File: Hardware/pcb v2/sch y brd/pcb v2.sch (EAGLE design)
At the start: 60 parts, among them J1 AVR_SPI_PRG_6PTH, J2 1981584-1, J3 HDMI, J4 HDMI, J5 JST-3, Q1 PMBT3904, Q2 PMBT3904, Q4 MC-306, U1 ATMEGA328P, U2 TXS0108EPWR-TSSOP20, U3 MB85RS16N, U4 ADP3338AKCZ-3.3RL7, U5 DS1307SO8, U6 BATTERYBATTERY1225_SMT, Y2 CSTCE16M0V53-R0 16MHZ

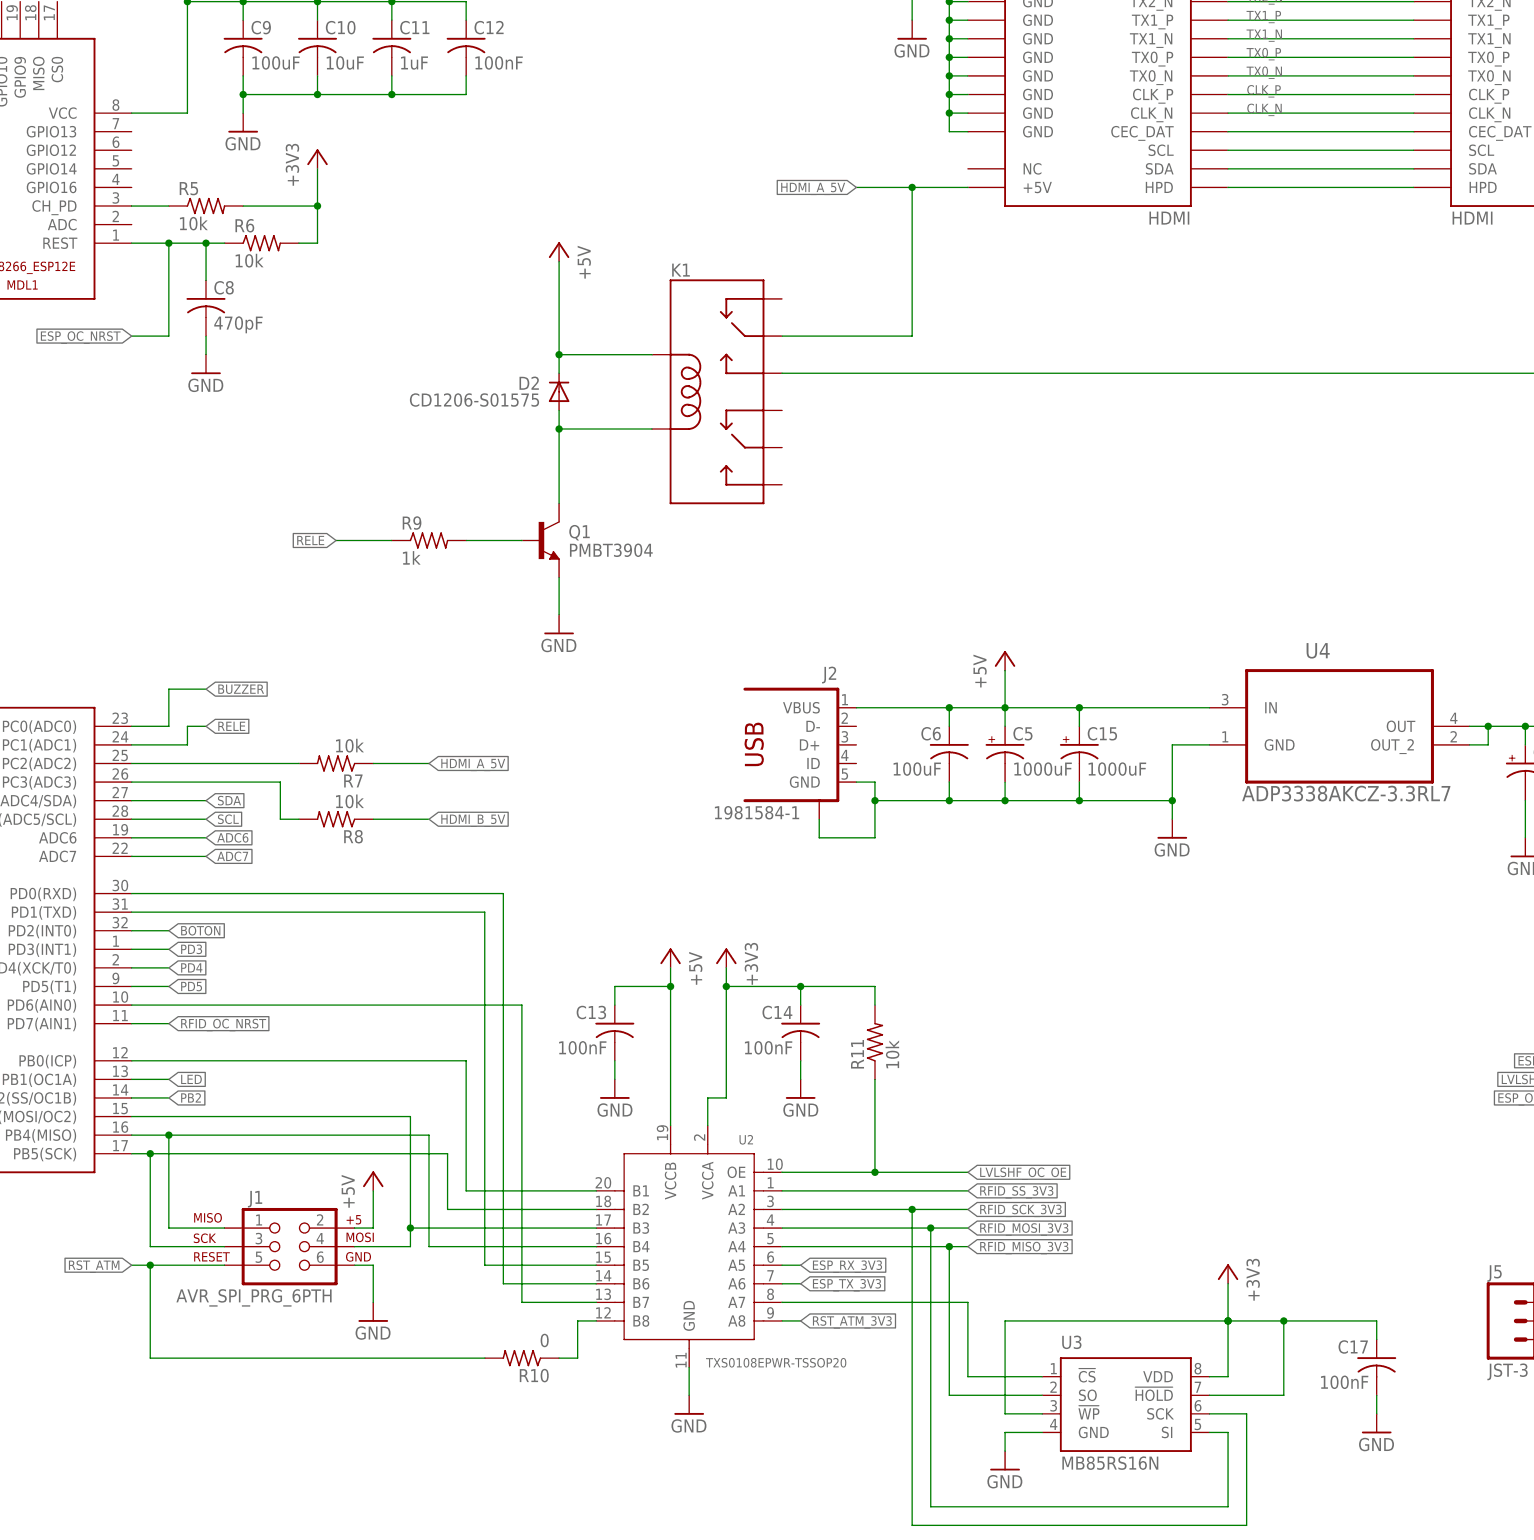
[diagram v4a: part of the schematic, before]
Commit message: ruteo hdmi completo
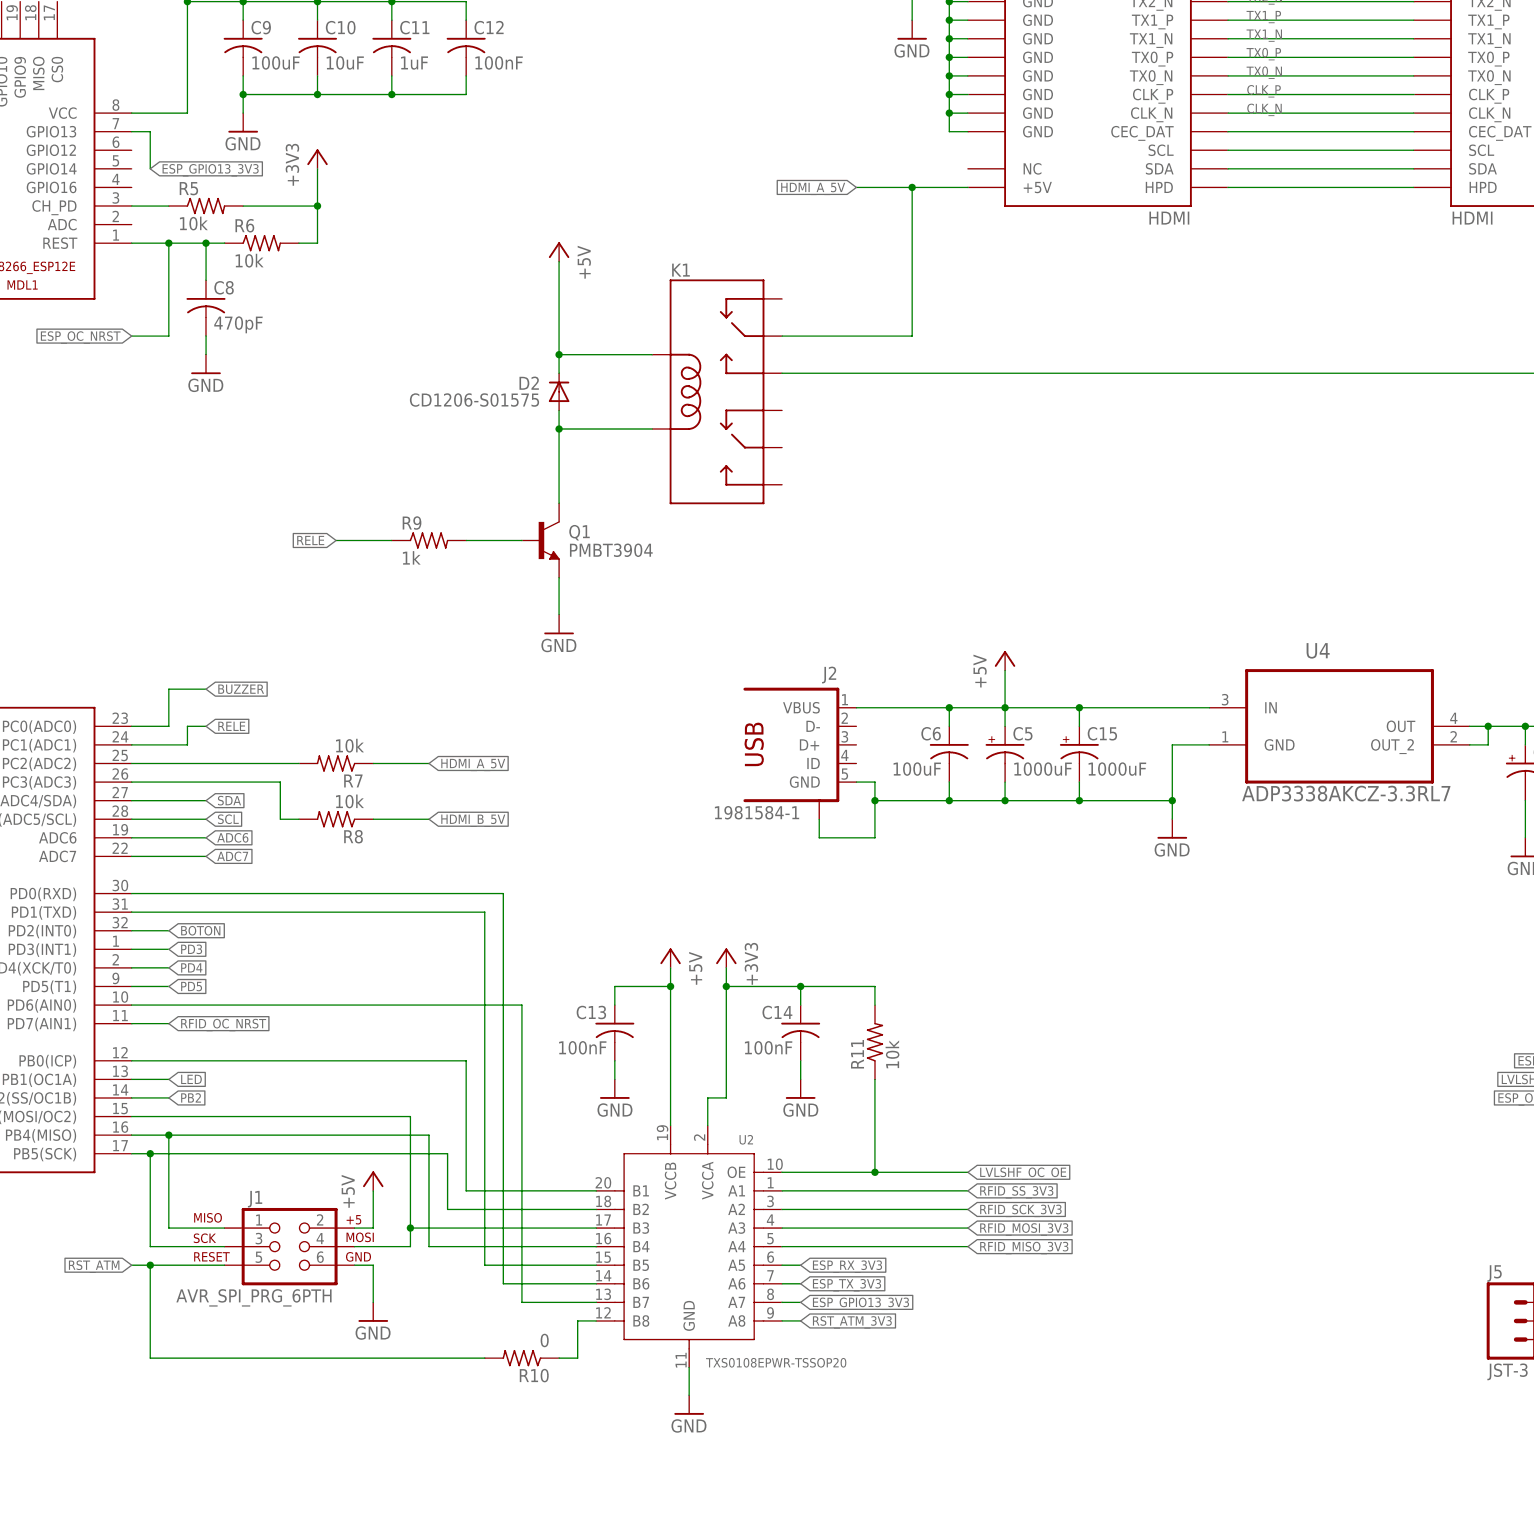
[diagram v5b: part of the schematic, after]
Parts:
- removed C17: 100nF, rcl:C-USC0805
- removed U3: MB85RS16N, partes v2:MB85RS16N
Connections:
- removed net N$39: U2.A7, U3.!CS
- new net ESP_GPIO13_3V3: MDL1.GPIO13, U2.A7
- net +3V3: no longer C17.1, U3.!HOLD, U3.!WP, U3.VDD
- net GND: no longer C17.2, U3.GND
- net RFID_MISO_3V3: no longer U3.SO
- net RFID_MOSI_3V3: no longer U3.SI
- net RFID_SCK_3V3: no longer U3.SCK
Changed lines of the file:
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@@
 <part name="GND18" library="supply1" deviceset="GND" device=""/>
 <part name="R8" library="rcl" deviceset="R-US_" device="R0805" value="10k"/>
-<part name="U3" library="partes v2" deviceset="MB85RS16N" device=""/>
-<part name="+3V35" library="supply1" deviceset="+3V3" device=""/>
-<part name="GND13" library="supply1" deviceset="GND" device=""/>
-<part name="C17" library="rcl" deviceset="C-US" device="C0805" value="100nF"/>
-<part name="GND15" library="supply1" deviceset="GND" device=""/>
 <part name="S1" library="SparkFun-Electromechanical" deviceset="SWITCH-MOMENTARY-2" device="SMD"/>
 <part name="GND25" library="supply1" deviceset="GND" device=""/>
@@
 <instance part="GND18" gate="1" x="335.28" y="185.42"/>
 <instance part="R8" gate="G$1" x="144.78" y="78.74" rot="R180"/>
-<instance part="U3" gate="G$1" x="251.46" y="-2.54"/>
-<instance part="+3V35" gate="G$1" x="266.7" y="17.78" rot="MR0"/>
-<instance part="GND13" gate="1" x="236.22" y="-10.16"/>
-<instance part="C17" gate="G$1" x="287.02" y="5.08" rot="MR0"/>
-<instance part="GND15" gate="1" x="287.02" y="-5.08"/>
 <instance part="S1" gate="G$1" x="441.96" y="93.98" smashed="yes" rot="R270">
 <attribute name="NAME" x="444.5" y="96.52" size="1.778" layer="95" rot="R270"/>
@@
 </segment>
 <segment>
-<pinref part="C17" gate="G$1" pin="2"/>
-<pinref part="GND15" gate="1" pin="GND"/>
-<wire x1="287.02" y1="0" x2="287.02" y2="-2.54" width="0.1524" layer="91"/>
-</segment>
-<segment>
-<pinref part="GND13" gate="1" pin="GND"/>
-<pinref part="U3" gate="G$1" pin="GND"/>
-<wire x1="236.22" y1="-7.62" x2="236.22" y2="-5.08" width="0.1524" layer="91"/>
-<wire x1="236.22" y1="-5.08" x2="241.3" y2="-5.08" width="0.1524" layer="91"/>
-</segment>
-<segment>
 <pinref part="S1" gate="G$1" pin="2"/>
 <pinref part="GND25" gate="1" pin="GND"/>
@@
 <segment>
 <pinref part="U2" gate="G$1" pin="A4"/>
-<wire x1="205.74" y1="20.32" x2="228.6" y2="20.32" width="0.1524" layer="91"/>
+<wire x1="205.74" y1="20.32" x2="231.14" y2="20.32" width="0.1524" layer="91"/>
 <label x="231.14" y="20.32" size="1.27" layer="95" xref="yes"/>
-<pinref part="U3" gate="G$1" pin="SO"/>
-<wire x1="228.6" y1="20.32" x2="231.14" y2="20.32" width="0.1524" layer="91"/>
-<wire x1="241.3" y1="0" x2="228.6" y2="0" width="0.1524" layer="91"/>
-<wire x1="228.6" y1="0" x2="228.6" y2="20.32" width="0.1524" layer="91"/>
-<junction x="228.6" y="20.32"/>
 </segment>
 <segment>
@@
 <segment>
 <pinref part="U2" gate="G$1" pin="A3"/>
-<wire x1="205.74" y1="22.86" x2="226.06" y2="22.86" width="0.1524" layer="91"/>
+<wire x1="205.74" y1="22.86" x2="231.14" y2="22.86" width="0.1524" layer="91"/>
 <label x="231.14" y="22.86" size="1.27" layer="95" xref="yes"/>
-<pinref part="U3" gate="G$1" pin="SI"/>
-<wire x1="226.06" y1="22.86" x2="231.14" y2="22.86" width="0.1524" layer="91"/>
-<wire x1="264.16" y1="-5.08" x2="266.7" y2="-5.08" width="0.1524" layer="91"/>
-<wire x1="266.7" y1="-5.08" x2="266.7" y2="-15.24" width="0.1524" layer="91"/>
-<wire x1="266.7" y1="-15.24" x2="226.06" y2="-15.24" width="0.1524" layer="91"/>
-<wire x1="226.06" y1="-15.24" x2="226.06" y2="22.86" width="0.1524" layer="91"/>
-<junction x="226.06" y="22.86"/>
 </segment>
 <segment>
@@
 <segment>
 <pinref part="U2" gate="G$1" pin="A2"/>
-<wire x1="205.74" y1="25.4" x2="223.52" y2="25.4" width="0.1524" layer="91"/>
+<wire x1="205.74" y1="25.4" x2="231.14" y2="25.4" width="0.1524" layer="91"/>
 <label x="231.14" y="25.4" size="1.27" layer="95" xref="yes"/>
-<pinref part="U3" gate="G$1" pin="SCK"/>
-<wire x1="223.52" y1="25.4" x2="231.14" y2="25.4" width="0.1524" layer="91"/>
-<wire x1="264.16" y1="-2.54" x2="269.24" y2="-2.54" width="0.1524" layer="91"/>
-<wire x1="269.24" y1="-2.54" x2="269.24" y2="-17.78" width="0.1524" layer="91"/>
-<wire x1="269.24" y1="-17.78" x2="223.52" y2="-17.78" width="0.1524" layer="91"/>
-<wire x1="223.52" y1="-17.78" x2="223.52" y2="25.4" width="0.1524" layer="91"/>
-<junction x="223.52" y="25.4"/>
 </segment>
 <segment>
@@
 </segment>
 <segment>
-<pinref part="+3V35" gate="G$1" pin="+3V3"/>
-<wire x1="266.7" y1="15.24" x2="266.7" y2="10.16" width="0.1524" layer="91"/>
-<wire x1="266.7" y1="10.16" x2="274.32" y2="10.16" width="0.1524" layer="91"/>
-<pinref part="C17" gate="G$1" pin="1"/>
-<wire x1="274.32" y1="10.16" x2="287.02" y2="10.16" width="0.1524" layer="91"/>
-<wire x1="287.02" y1="10.16" x2="287.02" y2="7.62" width="0.1524" layer="91"/>
-<pinref part="U3" gate="G$1" pin="VDD"/>
-<wire x1="266.7" y1="10.16" x2="266.7" y2="2.54" width="0.1524" layer="91"/>
-<wire x1="266.7" y1="2.54" x2="264.16" y2="2.54" width="0.1524" layer="91"/>
-<junction x="266.7" y="10.16"/>
-<junction x="266.7" y="10.16"/>
-<junction x="274.32" y="10.16"/>
-<pinref part="U3" gate="G$1" pin="!WP"/>
-<wire x1="236.22" y1="-2.54" x2="241.3" y2="-2.54" width="0.1524" layer="91"/>
-<wire x1="236.22" y1="-2.54" x2="236.22" y2="10.16" width="0.1524" layer="91"/>
-<wire x1="236.22" y1="10.16" x2="266.7" y2="10.16" width="0.1524" layer="91"/>
-<pinref part="U3" gate="G$1" pin="!HOLD"/>
-<wire x1="264.16" y1="0" x2="274.32" y2="0" width="0.1524" layer="91"/>
-<wire x1="274.32" y1="0" x2="274.32" y2="10.16" width="0.1524" layer="91"/>
-</segment>
-<segment>
 <pinref part="+3V38" gate="G$1" pin="+3V3"/>
 <wire x1="398.78" y1="30.48" x2="398.78" y2="22.86" width="0.1524" layer="91"/>
@@
 </segment>
 </net>
-<net name="N$39" class="0">
-<segment>
-<pinref part="U3" gate="G$1" pin="!CS"/>
-<wire x1="241.3" y1="2.54" x2="231.14" y2="2.54" width="0.1524" layer="91"/>
-<wire x1="231.14" y1="2.54" x2="231.14" y2="12.7" width="0.1524" layer="91"/>
-<pinref part="U2" gate="G$1" pin="A7"/>
-<wire x1="231.14" y1="12.7" x2="205.74" y2="12.7" width="0.1524" layer="91"/>
-</segment>
-</net>
 <net name="N$41" class="0">
 <segment>
@@
 </segment>
 </net>
+<net name="ESP_GPIO13_3V3" class="0">
+<segment>
+<pinref part="MDL1" gate="G$1" pin="GPIO13"/>
+<wire x1="116.84" y1="172.72" x2="119.38" y2="172.72" width="0.1524" layer="91"/>
+<wire x1="119.38" y1="172.72" x2="119.38" y2="167.64" width="0.1524" layer="91"/>
+<label x="119.38" y="167.64" size="1.27" layer="95" xref="yes"/>
+</segment>
+<segment>
+<pinref part="U2" gate="G$1" pin="A7"/>
+<wire x1="205.74" y1="12.7" x2="208.28" y2="12.7" width="0.1524" layer="91"/>
+<label x="208.28" y="12.7" size="1.27" layer="95" xref="yes"/>
+</segment>
+</net>

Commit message: avance ruteo
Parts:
- removed C20: 100nF, rcl:C-USC0805
- removed JP4: 2X6 FEMALE, SparkFun-Connectors:M06X2PTH_FEMALE
- removed U5: DS1307SO8, SparkFun-FreqCtrl:DS1307SO8
- removed U6: BATTERYBATTERY1225_SMT, seeedleo:BATTERYBATTERY1225_SMT
- added BT1: 1225BAT, partes v2:1225BAT
- added C18: 100nF, rcl:C-USC0603
- added JP1: FEMALE 2x3, SparkFun-Connectors:M03X2FEMALE
- added U3: ADP3338AKCZ-3.3RL7, ADI-Phase-2:ADP3338AKCZ-3.3RL7
- C1, C12, C2, C3, C4: device rcl:C-USC0805 -> rcl:C-USC0603
- C10: value 10uF -> 100nF; device rcl:C-USC1206 -> rcl:C-USC0603
- C11: value 1uF -> 100nF; device rcl:C-USC1206 -> rcl:C-USC0603
- C13, C7: value 100nF -> 100uF; device rcl:C-USC0805 -> rcl:C-USC1206
- C14: value 100nF -> 1200uF; device rcl:C-USC0805 -> rcl:CPOL-USUD-10X10
- C15: value 1000uF -> 1200uF
- C16: value (none) -> 10uF
- C5: value 1000uF -> 100nF; device rcl:CPOL-USUD-10X10 -> rcl:C-USC0603
- C6: value 100uF -> 470pF; device rcl:C-USC0805 -> rcl:C-USC0603
- C8: value 470pF -> 10uF; device rcl:C-USC1206 -> rcl:C-USC0805
- C9: value 100uF -> 1uF; device rcl:C-USC1206 -> rcl:C-USC0805
- J4: value HDMI -> JST-3; device partes v2:HDMI -> partes v2:JST-3
- J5: value JST-3 -> HDMI; device partes v2:JST-3 -> partes v2:HDMI
- JP2: value FEMALE 2x3 -> 2X6 FEMALE; device SparkFun-Connectors:M03X2FEMALE -> SparkFun-Connectors:M06X2PTH_FEMALE
- R11, R16, R17, R2, R3, R4, R5, R6, R7, R8: device rcl:R-US_R0805 -> rcl:R-US_R0603
- R14: value 4.7k -> 10k; device rcl:R-US_R0805 -> rcl:R-US_R0603
- U4: value ADP3338AKCZ-3.3RL7 -> DS1307SO8; device ADI-Phase-2:ADP3338AKCZ-3.3RL7 -> SparkFun-FreqCtrl:DS1307SO8
- renumbered C19 to C17, Q4 to Q3, Y2 to Y1
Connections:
- net +3V3: now also C7.1, C8.1, JP2.7, U3.OUT, U3.OUT_2; no longer C11.1, C14.1, JP4.7, U4.OUT, U4.OUT_2
- net +5V: now also C11.1, C14.+, C18.1, J4.3, JP2.9, U3.IN, U4.VCC; no longer C20.1, C5.+, C6.1, J5.3, JP4.9, U4.IN, U5.VCC
- net ADC6: now also JP2.3; no longer JP4.3
- net ADC7: now also JP2.5; no longer JP4.5
- net CLK_N: now also J5.CLK_N; no longer J4.CLK_N
- net CLK_P: now also J5.CLK_P; no longer J4.CLK_P
- net ESP_OC_NPROG: now also JP1.5; no longer JP2.5
- net ESP_OC_NRST: now also C6.1, JP1.4; no longer C8.1, JP2.4
- net ESP_RX_3V3: now also JP1.1; no longer JP2.1
- net ESP_TX_3V3: now also JP1.2; no longer JP2.2
- net GND: now also BT1.V-, C14.-, C18.2, C5.2, J4.1, J5.GND@1, J5.GND@2, J5.GND@3, J5.GND@4, J5.GND@5, J5.GND@6, J5.GND@7, J5.GND@8, J5.GND@9, JP1.6, JP2.11, JP2.2, U3.GND; no longer C14.2, C20.2, C5.-, J4.GND@1, J4.GND@2, J4.GND@3, J4.GND@4, J4.GND@5, J4.GND@6, J4.GND@7, J4.GND@8, J4.GND@9, J5.1, JP2.6, JP4.11, JP4.2, U5.GND, U6.-
- net HDMI_B_5V: now also J5.+5V; no longer J4.+5V
- net LED: now also J4.2; no longer J5.2
- net LVLSHF_OC_OE: now also JP1.3; no longer JP2.3
- net N$2: now also U4.X1; no longer U5.X1
- net N$3: now also U4.X2; no longer U5.X2
- net N$30: now also J5.CEC_DAT; no longer J4.CEC_DAT
- net N$31: now also J5.SCL; no longer J4.SCL
- net N$32: now also J5.SDA; no longer J4.SDA
- net N$33: now also J5.HPD; no longer J4.HPD
- net N$6: now also U4.SQW; no longer U5.SQW
- net N$9: now also BT1.V+, U4.VBATT; no longer U5.VBATT, U6.+
- net PB2: now also JP2.6; no longer JP4.6
- net PD3: now also JP2.1; no longer JP4.1
- net PD4: now also JP2.12; no longer JP4.12
- net PD5: now also JP2.4; no longer JP4.4
- net RST_ATM: now also C5.1; no longer C7.1
- net SCL: now also JP2.10, U4.SCL; no longer JP4.10, U5.SCL
- net SDA: now also JP2.8, U4.SDA; no longer JP4.8, U5.SDA
- net TX0_N: now also J5.TX0_N; no longer J4.TX0_N
- net TX0_P: now also J5.TX0_P; no longer J4.TX0_P
- net TX1_N: now also J5.TX1_N; no longer J4.TX1_N
- net TX1_P: now also J5.TX1_P; no longer J4.TX1_P
- net TX2_N: now also J5.TX2_N; no longer J4.TX2_N
- net TX2_P: now also J5.TX2_P; no longer J4.TX2_P
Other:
- moved on the sheet: C10, C11, C12, C13, C6, C7, C8, C9
